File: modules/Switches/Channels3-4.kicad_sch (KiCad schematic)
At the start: 34 parts, among them Q1 2N3906, Q2 J109, Q3 J109, Q4 2N3906, Q5 J109, Q6 J109, U1 TL074, U2 SN74HCS74

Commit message: Switches - PCB layout - wip
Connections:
- net MUTE-3: now reaches C12.1, Q2.3 (G), Q3.3 (G), R8.2
- net MUTE-4: now reaches C13.1, Q5.3 (G), Q6.3 (G), R19.2
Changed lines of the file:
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@@
   (junction (at 133.35 72.39) (diameter 0) (color 0 0 0 0)
   )
+  (junction (at 144.78 143.51) (diameter 0) (color 0 0 0 0)
+  )
   (junction (at 114.3 151.13) (diameter 0) (color 0 0 0 0)
   )
@@
   (junction (at 133.35 151.13) (diameter 0) (color 0 0 0 0)
   )
+  (junction (at 144.78 64.77) (diameter 0) (color 0 0 0 0)
+  )
   (junction (at 102.87 119.38) (diameter 0) (color 0 0 0 0)
   )
@@
     (stroke (width 0) (type default))
   )
-  (wire (pts (xy 149.86 143.51) (xy 135.89 143.51))
+  (wire (pts (xy 144.78 64.77) (xy 135.89 64.77))
+    (stroke (width 0) (type default))
+  )
+  (wire (pts (xy 149.86 143.51) (xy 144.78 143.51))
     (stroke (width 0) (type default))
   )
@@
     (stroke (width 0) (type default))
   )
+  (wire (pts (xy 144.78 60.96) (xy 144.78 64.77))
+    (stroke (width 0) (type default))
+  )
   (wire (pts (xy 186.69 124.46) (xy 187.96 124.46))
     (stroke (width 0) (type default))
@@
     (stroke (width 0) (type default))
   )
+  (wire (pts (xy 146.05 139.7) (xy 144.78 139.7))
+    (stroke (width 0) (type default))
+  )
   (wire (pts (xy 157.48 43.18) (xy 162.56 43.18))
     (stroke (width 0) (type default))
@@
     (stroke (width 0) (type default))
   )
+  (wire (pts (xy 144.78 143.51) (xy 135.89 143.51))
+    (stroke (width 0) (type default))
+  )
   (wire (pts (xy 102.87 120.65) (xy 102.87 119.38))
     (stroke (width 0) (type default))
@@
     (stroke (width 0) (type default))
   )
+  (wire (pts (xy 144.78 139.7) (xy 144.78 143.51))
+    (stroke (width 0) (type default))
+  )
   (wire (pts (xy 161.29 48.26) (xy 161.29 54.61))
     (stroke (width 0) (type default))
@@
     (stroke (width 0) (type default))
   )
+  (wire (pts (xy 146.05 60.96) (xy 144.78 60.96))
+    (stroke (width 0) (type default))
+  )
   (wire (pts (xy 77.47 128.27) (xy 77.47 140.97))
     (stroke (width 0) (type default))
@@
     (stroke (width 0) (type default))
   )
-  (wire (pts (xy 149.86 64.77) (xy 135.89 64.77))
+  (wire (pts (xy 149.86 64.77) (xy 144.78 64.77))
     (stroke (width 0) (type default))
   )
@@
   (text "Channel 4" (at 46.99 110.49 0)
     (effects (font (size 1.27 1.27) (thickness 0.254) bold) (justify left bottom))
+  )
+  (global_label "MUTE-4" (shape output) (at 146.05 139.7 0) (fields_autoplaced)
+    (effects (font (size 1.27 1.27)) (justify left))
+    (property "Intersheetrefs" "${INTERSHEET_REFS}" (at 156.0614 139.7 0)
+      (effects (font (size 1.27 1.27)) (justify left) hide)
+    )
   )
   (global_label "LED-4" (shape output) (at 99.06 151.13 0) (fields_autoplaced)
@@
     )
   )
+  (global_label "MUTE-3" (shape output) (at 146.05 60.96 0) (fields_autoplaced)
+    (effects (font (size 1.27 1.27)) (justify left))
+    (property "Intersheetrefs" "${INTERSHEET_REFS}" (at 156.0614 60.96 0)
+      (effects (font (size 1.27 1.27)) (justify left) hide)
+    )
+  )

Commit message: Switches - PCB layout - routing done
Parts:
- R1, R15: footprint -lmp-misc:R_Axial_DIN0207_L6.3mm_D2.5mm_P10.16mm_Horizontal -> -lmp-misc:R_Axial_DIN0207_L6.3mm_D2.5mm_P7.62mm_Horizontal
- R22: footprint -lmp-misc:R_Axial_DIN0207_L6.3mm_D2.5mm_P10.16mm_Horizontal -> -lmp-stripboard:SB_Gen_1
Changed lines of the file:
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@@
       (effects (font (size 1.27 1.27)))
     )
-    (property "Footprint" "-lmp-misc:R_Axial_DIN0207_L6.3mm_D2.5mm_P10.16mm_Horizontal" (at 93.98 70.612 90)
+    (property "Footprint" "-lmp-misc:R_Axial_DIN0207_L6.3mm_D2.5mm_P7.62mm_Horizontal" (at 93.98 70.612 90)
       (effects (font (size 1.27 1.27)) hide)
     )
@@
       (effects (font (size 1.27 1.27)))
     )
-    (property "Footprint" "-lmp-misc:R_Axial_DIN0207_L6.3mm_D2.5mm_P10.16mm_Horizontal" (at 93.98 149.352 90)
+    (property "Footprint" "-lmp-misc:R_Axial_DIN0207_L6.3mm_D2.5mm_P7.62mm_Horizontal" (at 93.98 149.352 90)
       (effects (font (size 1.27 1.27)) hide)
     )
@@
       (effects (font (size 1.27 1.27)))
     )
-    (property "Footprint" "-lmp-misc:R_Axial_DIN0207_L6.3mm_D2.5mm_P10.16mm_Horizontal" (at 182.88 126.238 90)
-      (effects (font (size 1.27 1.27)) hide)
-    )
+    (property "Footprint" "-lmp-stripboard:SB_Gen_1" (at 182.88 126.238 90)
+      (effects (font (size 1.27 1.27)) hide)
+    )

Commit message: Switches - PCB layout, BOM - wip
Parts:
- Q2, Q3, Q5, Q6: Distributor (none) -> Mouser; DistributorPartLink (none) -> https://www.mouser.ca/ProductDetail/512-J109_D26Z; DistributorPartNum (none) -> 512-J109_D26Z; Manufacturer (none) -> onsemi / Fairchild; ManufacturerPartNum (none) -> J109-D26Z
- R1, R15: DistributorPartLink https://www.mouser.ca/ProductDetail/Vishay-Dale/CCF071K00JK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 -> https://www.mouser.ca/ProductDetail/603-MFR-12FTF52-330R; DistributorPartNum 71-CCF071K00JKE36 -> 603-MFR-12FTF52-330R; Manufacturer Vishay / Dale -> YAGEO; ManufacturerPartNum CCF071K00JKE36 -> MFR-12FTF52-330R
- R10, R12, R13, R17, R18, R2, R20, R21, R4, R6, R7, R9: DistributorPartLink https://www.mouser.ca/c/?m=YAGEO&power+rating=166+mW+(1%2f6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 -> https://www.mouser.ca/ProductDetail/YAGEO/MFR-12FTF52-10K?q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; DistributorPartNum 603-MFR-12* -> 603-MFR-12FTF52-10K; ManufacturerPartNum MFR-12* -> MFR-12FTF52-10K
- R14, R3: DistributorPartLink https://www.mouser.ca/c/?m=YAGEO&power+rating=166+mW+(1%2f6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 -> https://www.mouser.ca/ProductDetail/YAGEO/MFR-12FTF52-1K?qs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; DistributorPartNum 603-MFR-12* -> 603-MFR-12FTF52-1K; ManufacturerPartNum MFR-12* -> MFR-12FTF52-1K
- R16, R5: DistributorPartLink https://www.mouser.ca/c/?m=YAGEO&power+rating=166+mW+(1%2f6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 -> https://www.mouser.ca/ProductDetail/YAGEO/MFR-12FTF52-100K?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; DistributorPartNum 603-MFR-12* -> 603-MFR-12FTF52-100K; ManufacturerPartNum MFR-12* -> MFR-12FTF52-100K
- R19, R8: DistributorPartLink https://www.mouser.ca/c/?m=YAGEO&power+rating=166+mW+(1%2f6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 -> https://www.mouser.ca/ProductDetail/YAGEO/MFR-12FTF52-240K?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; DistributorPartNum 603-MFR-12* -> 603-MFR-12FTF52-240K; ManufacturerPartNum MFR-12* -> MFR-12FTF52-240K

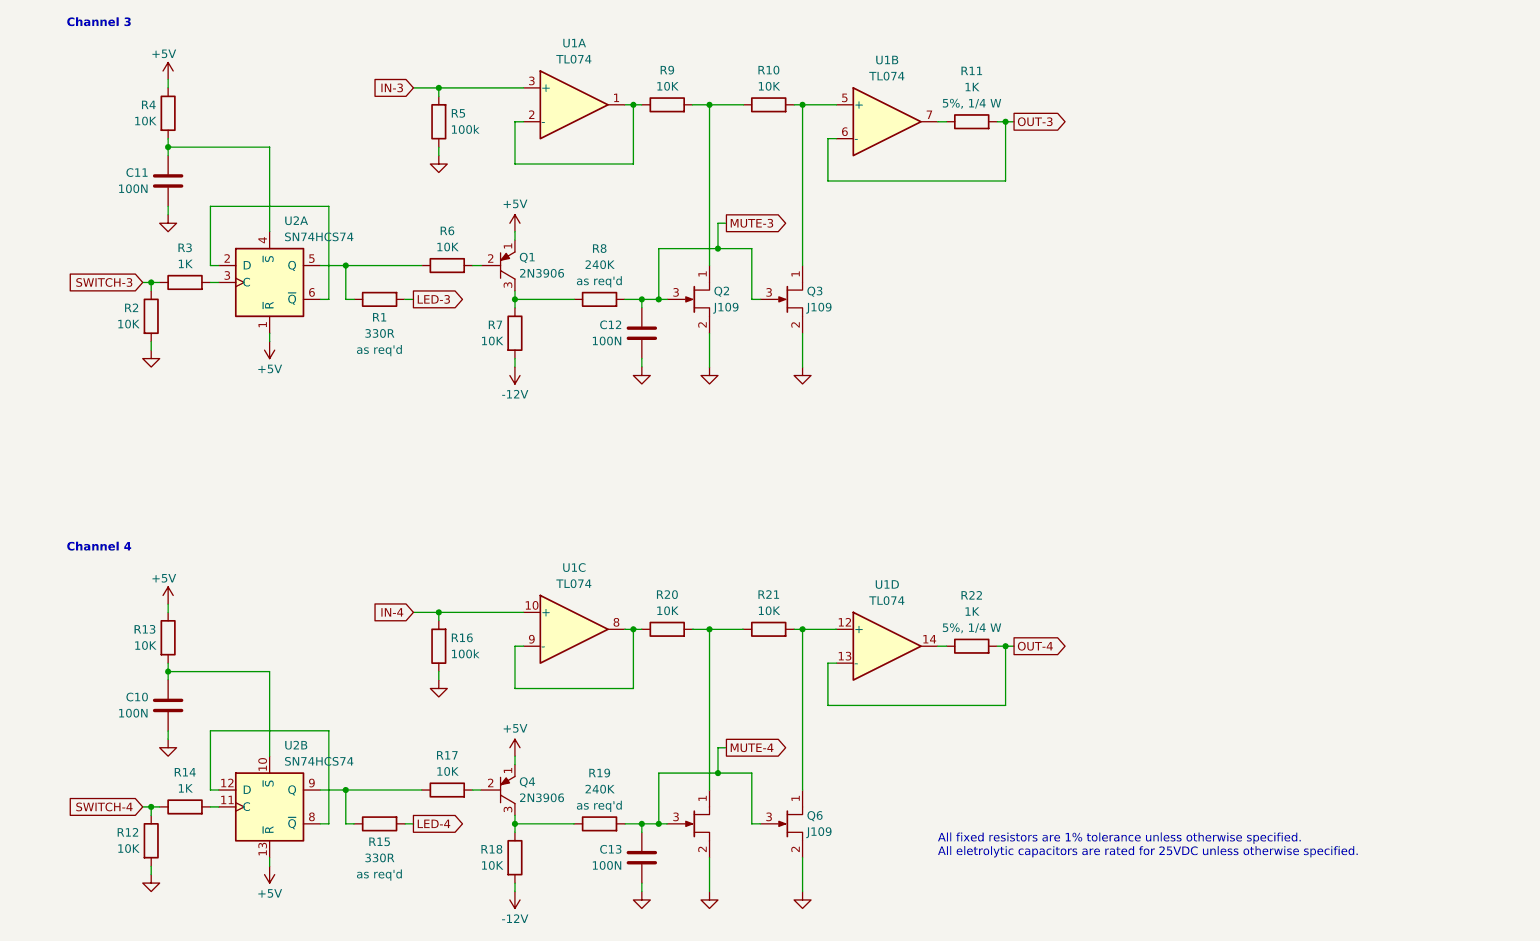
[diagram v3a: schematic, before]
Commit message: Switches - schematic notes
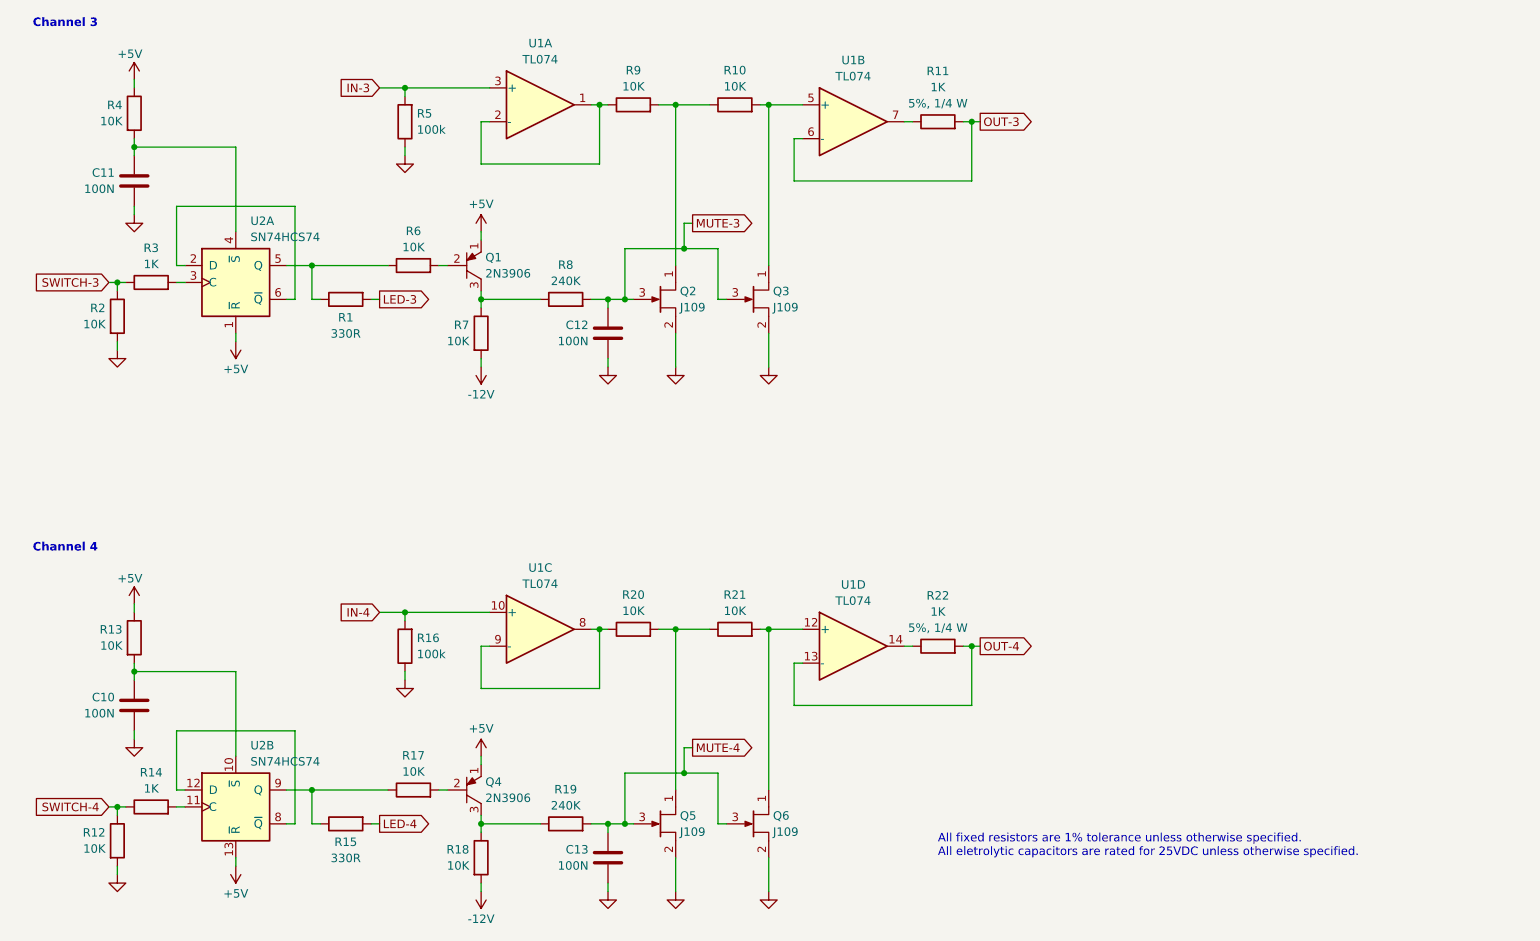
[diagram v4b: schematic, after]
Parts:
- R1, R15, R19, R8: Note as req'd -> (none)
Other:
- moved on the sheet: C10, C11, C12, C13, Q1, Q2, Q3, Q4, Q6, R1, R10, R11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
